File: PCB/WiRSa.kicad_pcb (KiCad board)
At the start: 2 copper layers, 43.2 x 26.7 mm, 3 parts, among them J1 RS232_TTL_Adapter, U1 WeMos_D1_mini

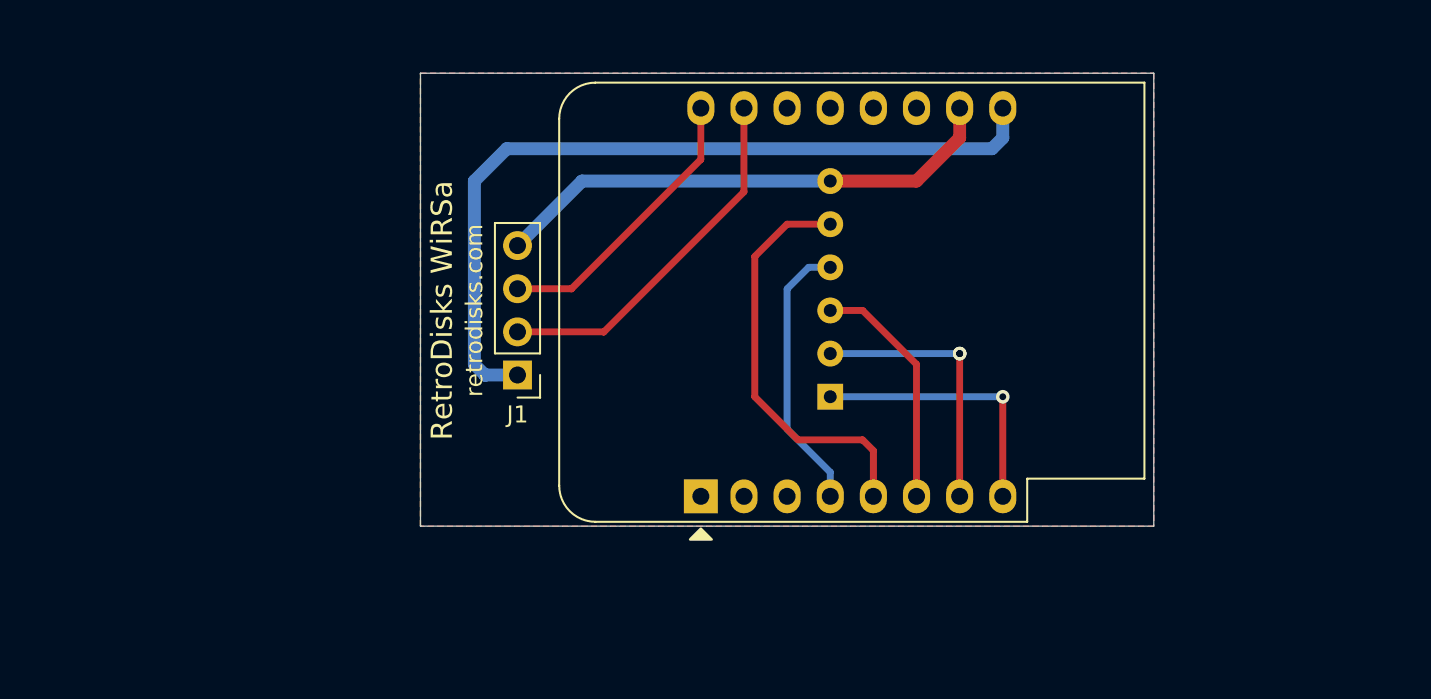
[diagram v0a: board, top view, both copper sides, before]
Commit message: v2 PCB update
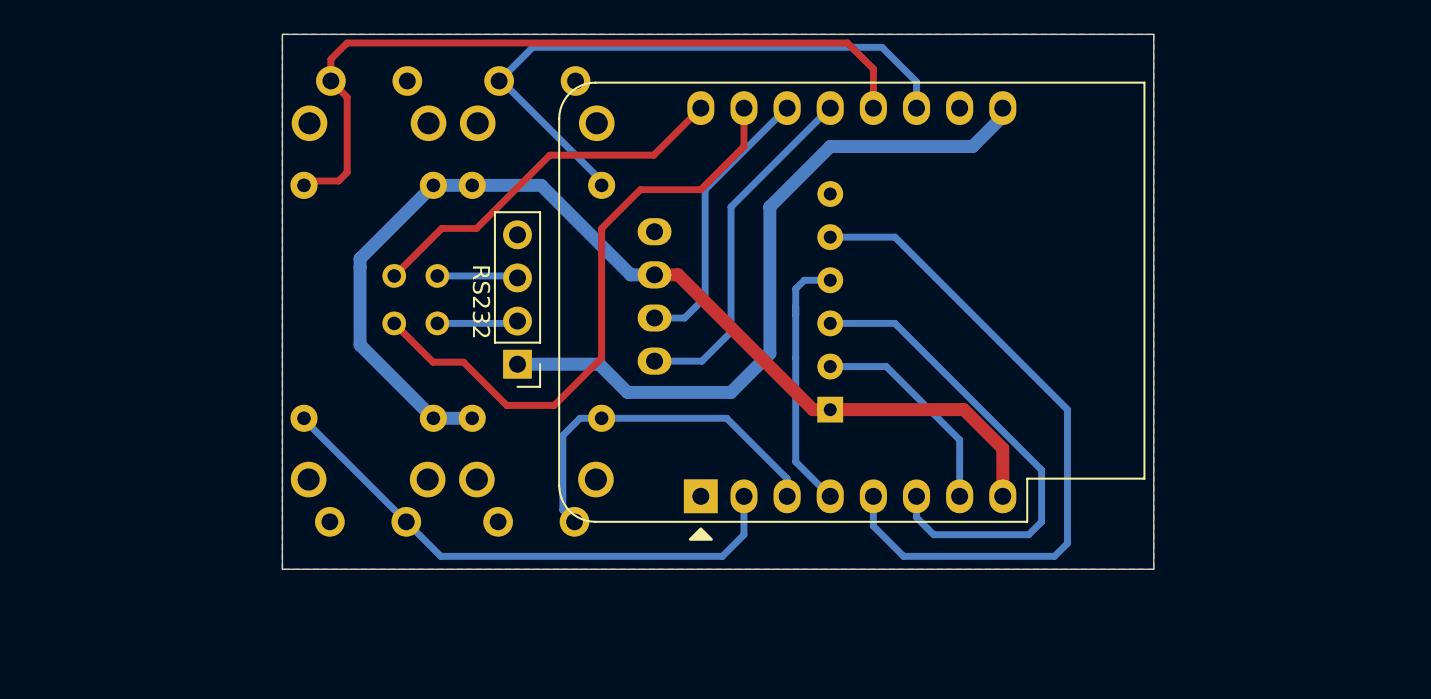
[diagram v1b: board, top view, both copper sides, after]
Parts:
- added Brd1: SSD1306, SSD1306:128x64OLED, B.Cu at (93.0, 87.9)
- added R1: 10k, Resistor_THT:R_Axial_DIN0207_L6.3mm_D2.5mm_P7.62mm_Horizontal, B.Cu at (69.3, 95.2)
- added R2: 10k, Resistor_THT:R_Axial_DIN0207_L6.3mm_D2.5mm_P7.62mm_Horizontal, B.Cu at (71.6, 95.2)
- added R3: 10k, Resistor_THT:R_Axial_DIN0207_L6.3mm_D2.5mm_P7.62mm_Horizontal, B.Cu at (69.3, 81.5)
- added R4: 10k, Resistor_THT:R_Axial_DIN0207_L6.3mm_D2.5mm_P7.62mm_Horizontal, B.Cu at (71.6, 81.5)
- added RX: RX, TestPoint:TestPoint_2Pads_Pitch2.54mm_Drill0.8mm, B.Cu at (69.6, 89.7)
- added SW1: SW_Push, Button_Switch_THT:SW_Tactile_SPST_Angled_PTS645Vx58-2LFS, B.Cu at (63.2, 101.3)
- added SW2: SW_Push, Button_Switch_THT:SW_Tactile_SPST_Angled_PTS645Vx58-2LFS, B.Cu at (73.2, 101.3)
- added SW3: SW_Push, Button_Switch_THT:SW_Tactile_SPST_Angled_PTS645Vx58-2LFS, B.Cu at (67.8, 75.4)
- added SW4: SW_Push, Button_Switch_THT:SW_Tactile_SPST_Angled_PTS645Vx58-2LFS, B.Cu at (77.7, 75.4)
- added TX: TX, TestPoint:TestPoint_2Pads_Pitch2.54mm_Drill0.8mm, B.Cu at (69.6, 86.9)
- moved A1 0.76 mm to (92.7, 94.7)
- moved RS232 0.64 mm to (74.3, 92.1)
- renumbered J1 to RS232
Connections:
- U1 pad 11: unconnected-(U1-Pad11) -> Net-(R4-Pad2)
- U1 pad 12: unconnected-(U1-Pad12) -> Net-(R3-Pad2)
- U1 pad 13: unconnected-(U1-Pad13) -> Net-(Brd1-Pad4)
- U1 pad 14: unconnected-(U1-Pad14) -> Net-(Brd1-Pad3)
- U1 pad 15: Net-(J1-Pad2) -> Net-(JP1-Pad2)
- U1 pad 16: Net-(J1-Pad3) -> Net-(JP2-Pad2)
- U1 pad 2: unconnected-(U1-Pad2) -> Net-(R1-Pad2)
- U1 pad 3: unconnected-(U1-Pad3) -> Net-(R2-Pad2)
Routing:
- net Net-(A1-Pad1): track 16.0 -> 62.3 mm, vias 1 -> 0
- net Net-(R3-Pad2): track 0.00 -> 45.1 mm
- net Net-(R4-Pad2): track 0.00 -> 36.3 mm
- net Net-(JP1-Pad2): track 0.00 -> 35.6 mm
- net Net-(R1-Pad2): track 0.00 -> 32.1 mm
- net GND: track 30.4 -> 0.00 mm
- net Net-(JP2-Pad2): track 0.00 -> 22.1 mm
- net Net-(R2-Pad2): track 0.00 -> 21.5 mm
- net Net-(Brd1-Pad4): track 0.00 -> 20.8 mm
- net Net-(J1-Pad2): track 21.7 -> 4.78 mm
- net Net-(Brd1-Pad3): track 0.00 -> 16.6 mm
- net Net-(A1-Pad5): track 24.5 -> 40.3 mm
- net Net-(A1-Pad3): track 14.2 -> 28.4 mm
- net Net-(J1-Pad3): track 17.0 -> 4.77 mm
- net Net-(J1-Pad1): track 47.5 -> 41.5 mm
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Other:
- board size 43.2 x 26.7 mm -> 51.3 x 31.5 mm
- board text added: "RetroDisks WiRSa v2"
- board text removed: "RetroDisks WiRSa"
- board text removed: "retrodisks.com"

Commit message: WiRSa v3.01
Initial push for the version 3 design
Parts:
- removed A1: SD_Card_Module, Charles:SD_Card_Module
- removed Brd1: SSD1306, SSD1306:128x64OLED
- removed RS232: RS232_TTL_Adapter, Connector_PinHeader_2.54mm:PinHeader_1x04_P2.54mm_Vertical
- removed RX: RX, TestPoint:TestPoint_2Pads_Pitch2.54mm_Drill0.8mm
- removed TX: TX, TestPoint:TestPoint_2Pads_Pitch2.54mm_Drill0.8mm
- added C1: 0.1uF, Capacitor_SMD:C_0603_1608Metric, F.Cu at (87.1, 91.1)
- added C2: 0.1uF, Capacitor_SMD:C_0603_1608Metric, F.Cu at (72.7, 89.9)
- added C3: 0.1uF, Capacitor_SMD:C_0603_1608Metric, F.Cu at (82.9, 88.0)
- added C4: 0.1uF, Capacitor_SMD:C_0603_1608Metric, F.Cu at (87.1, 95.0)
- added C5: 0.1uF, Capacitor_SMD:C_0603_1608Metric, F.Cu at (72.7, 92.5)
- added G***: LOGO, wirsa:retrodisks, B.Cu at (63.4, 92.6)
- added IC1: MAX3243CDBR, easyeda2kicad:SSOP-28_L10.2-W5.3-P0.65-LS7.8-BL, F.Cu at (80.0, 94.1)
- added J1: DE9 Female, Connector_Dsub:DSUB-9_Female_Horizontal_P2.77x2.84mm_EdgePinOffset4.94mm_Housed_MountingHolesOffset7.48mm, F.Cu at (54.7, 97.1)
- added J2: spare IO, Connector_PinHeader_2.54mm:PinHeader_1x02_P2.54mm_Vertical, F.Cu at (123.8, 83.1)
- added J3: Conn_01x02_Socket, Connector_PinHeader_2.54mm:PinHeader_1x02_P2.54mm_Vertical, F.Cu at (60.4, 76.5)
- added J4: 2016WVS-02P, easyeda2kicad:CONN-SMD_P2.00_X2016WVS-02-9TSW, F.Cu at (66.7, 78.9)
- added R5: 10k, Resistor_SMD:R_0603_1608Metric, F.Cu at (58.9, 99.4)
- added R6: 10k, Resistor_SMD:R_0603_1608Metric, F.Cu at (61.5, 99.4)
- added R7: 10k, Resistor_SMD:R_0603_1608Metric, F.Cu at (64.0, 99.4)
- added R8: 10k, Resistor_SMD:R_0603_1608Metric, F.Cu at (66.8, 99.4)
- added R9: 10k, Resistor_SMD:R_0603_1608Metric, F.Cu at (69.4, 99.4)
- added SW5: SK-3245S-L3-B, easyeda2kicad:SW-SMD_SK-3245S-L3-B, F.Cu at (77.1, 77.3)
- added U2: ESP32-WROOM-32D DEV BOARD, esp32:ESP32-C3-DevKitC-02, F.Cu at (62.5, 109.7)
- R1, R2, R3, R4: footprint Resistor_THT:R_Axial_DIN0207_L6.3mm_D2.5mm_P7.62mm_Horizontal -> Resistor_SMD:R_0603_1608Metric; moved to F.Cu
- SW1, SW2, SW3, SW4: moved to F.Cu
- U1: value WeMos_D1_mini -> TF-123-ARP9H17; footprint Module:WEMOS_D1_mini_light -> easyeda2kicad:TF-SMD_TF-123-ARP9H15
- moved R4 47.4 mm to (119.0, 80.6), turned to 180 degrees
- moved R3 39.9 mm to (109.2, 80.6), turned to 0 degrees
- moved SW4 38.6 mm to (116.3, 76.1), turned to 0 degrees
- moved SW3 38.6 mm to (106.4, 76.1), turned to 0 degrees
- moved SW2 34.4 mm to (96.5, 76.1)
- moved SW1 34.4 mm to (86.6, 76.1)
- moved R2 31.2 mm to (99.2, 80.6)
- moved R1 24.9 mm to (89.5, 80.6), turned to 0 degrees
- moved U1 21.8 mm to (64.2, 105.8), turned to 0 degrees
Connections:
- R1 pad 1: Net-(A1-Pad1) -> Net-(IC1-FORCEON)
- R1 pad 2: Net-(R1-Pad2) -> Net-(U2-D36/SENS_VP)
- R2 pad 1: Net-(A1-Pad1) -> Net-(IC1-FORCEON)
- R2 pad 2: Net-(R2-Pad2) -> Net-(U2-D39/SENS_VN)
- R3 pad 1: Net-(A1-Pad1) -> Net-(IC1-FORCEON)
- R3 pad 2: Net-(R3-Pad2) -> Net-(U2-D34)
- R4 pad 1: Net-(A1-Pad1) -> Net-(IC1-FORCEON)
- R4 pad 2: Net-(R4-Pad2) -> Net-(U2-D35)
- SW1 pad 2: Net-(R1-Pad2) -> Net-(U2-D36/SENS_VP)
- SW2 pad 2: Net-(R2-Pad2) -> Net-(U2-D39/SENS_VN)
- SW3 pad 2: Net-(R3-Pad2) -> Net-(U2-D34)
- SW4 pad 2: Net-(R4-Pad2) -> Net-(U2-D35)
- U1 pad 1: unconnected-(U1-Pad1) -> Net-(U1-DAT2)
- U1 pad 11: Net-(R4-Pad2) -> GND
- U1 pad 12: Net-(R3-Pad2) -> GND
- U1 pad 13: Net-(Brd1-Pad4) -> GND
- U1 pad 2: Net-(R1-Pad2) -> Net-(U1-CD/DAT3)
- U1 pad 3: Net-(R2-Pad2) -> Net-(U1-CMD)
- U1 pad 4: Net-(A1-Pad4) -> Net-(IC1-FORCEON)
- U1 pad 6: Net-(A1-Pad3) -> GND
- U1 pad 8: Net-(A1-Pad1) -> Net-(U1-DAT1)
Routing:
- net Net-(IC1-FORCEON): track 0.00 -> 101.3 mm
- net Net-(A1-Pad1): track 62.3 -> 0.00 mm
- net Net-(U2-D35): track 0.00 -> 56.5 mm
- net Net-(U2-D34): track 0.00 -> 49.4 mm
- net Net-(U2-D36/SENS_VP): track 0.00 -> 48.9 mm
- net /RTS-TI: track 0.00 -> 46.7 mm, vias 0 -> 1
- net Net-(R3-Pad2): track 45.1 -> 0.00 mm
- net Net-(U2-D39/SENS_VN): track 0.00 -> 43.6 mm, vias 0 -> 1
- net Net-(U1-CD/DAT3): track 0.00 -> 41.6 mm, vias 0 -> 1
- net /DSR-RI: track 0.00 -> 40.7 mm, vias 0 -> 1
- net Net-(U1-CLK): track 40.3 -> 0.00 mm
- net /RX-TO: track 0.00 -> 37.0 mm, vias 0 -> 1
- net Net-(U1-DAT0): track 12.7 -> 49.1 mm, vias 0 -> 1
- net Net-(R4-Pad2): track 36.3 -> 0.00 mm
- net Net-(JP1-Pad2): track 35.6 -> 0.00 mm
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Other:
- board size 51.3 x 31.5 mm -> 79.6 x 36.3 mm
- board text added: "+"
- board text added: "-"
- board text added: "BAT"
- board text added: "CTS (RI)"
- board text added: "DCD (RI)"
- board text added: "DSR (RI)"
- board text added: "DTR (RO)"
- board text added: "GND"
- board text added: "RI (RI)"
- board text added: "RTS (RO)"
- board text added: "RX (RI)"
- board text added: "RetroDisks WiRSa V3"
- board text added: "SPARE I/O"
- board text added: "TX (RO)"
- board text added: "WiRSa V3"
- board text removed: "RetroDisks WiRSa v2"
